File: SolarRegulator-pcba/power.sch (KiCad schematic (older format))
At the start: 59 parts

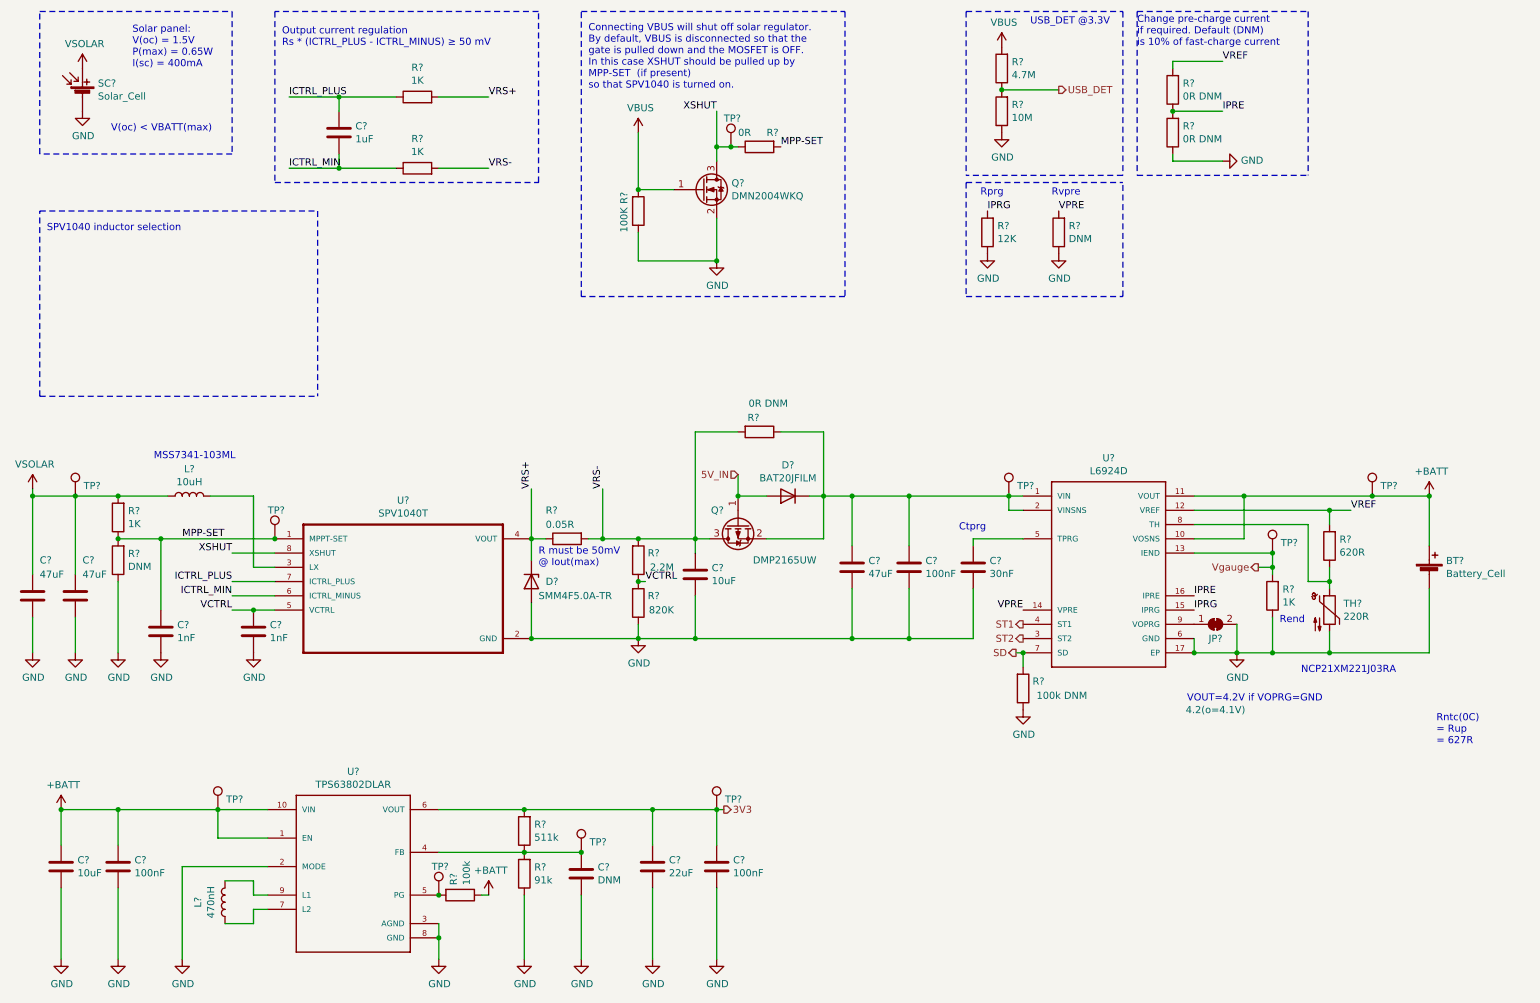
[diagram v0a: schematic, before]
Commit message: Add terminal blocks
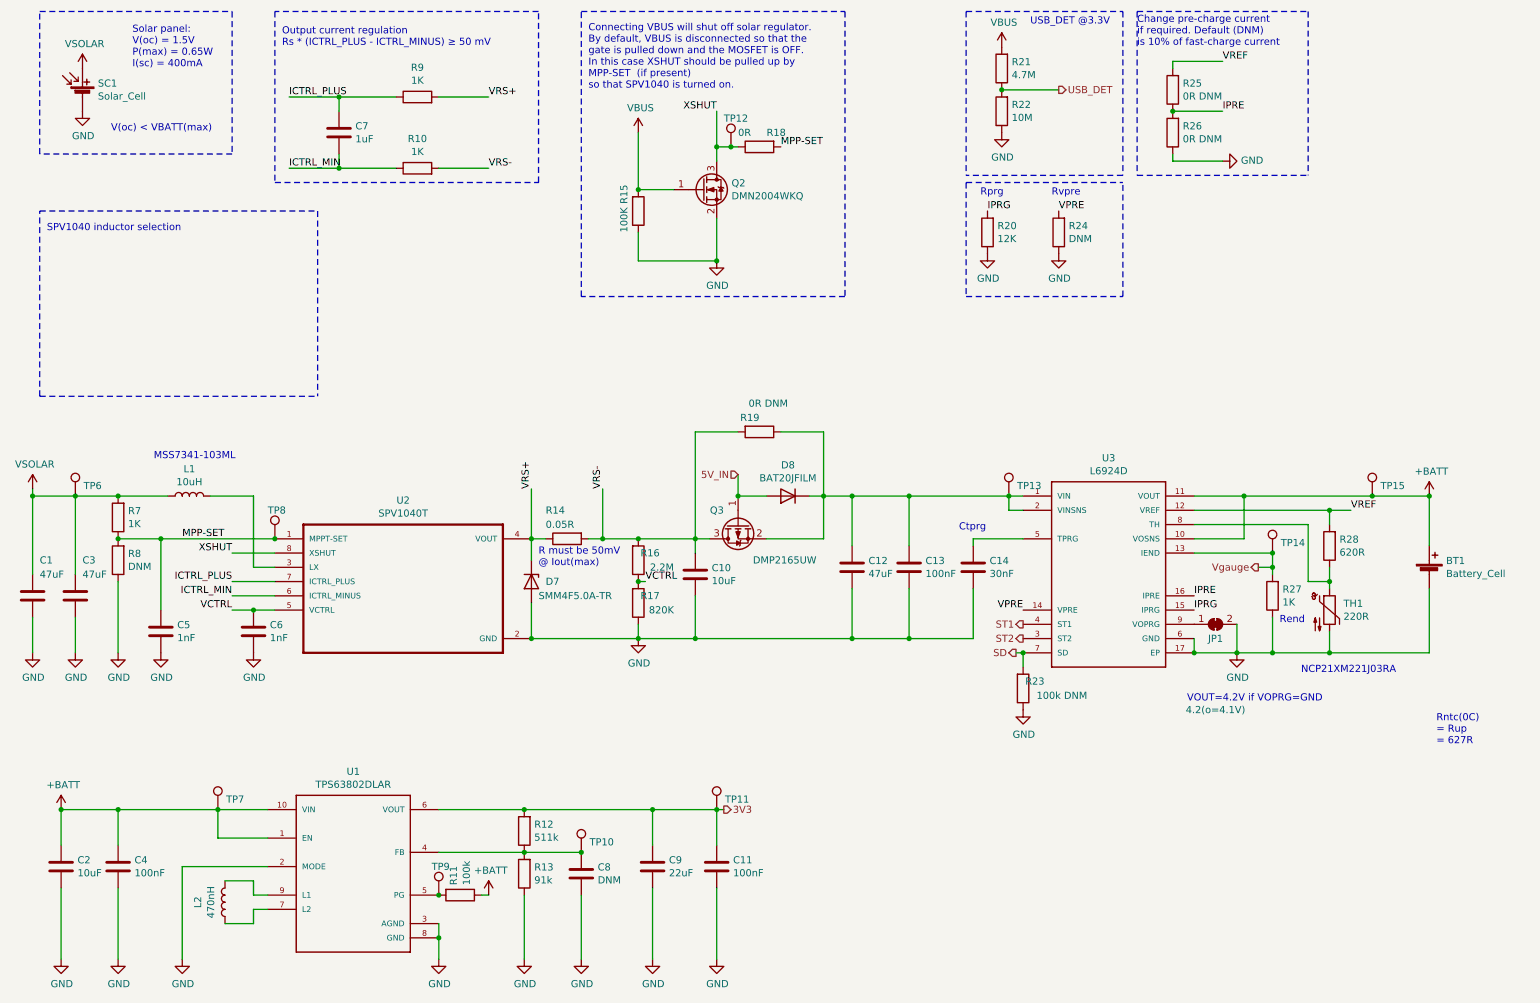
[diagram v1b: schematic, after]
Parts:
- BT1: renamed from BT?; footprint Connector_JST:JST_PH_S2B-PH-SM4-TB_1x02-1MP_P2.00mm_Horizontal -> TerminalBlock_Phoenix:TerminalBlock_Phoenix_MKDS-1,5-2_1x02_P5.00mm_Horizontal
- SC1: renamed from SC?; footprint Connector_JST:JST_PH_S2B-PH-SM4-TB_1x02-1MP_P2.00mm_Horizontal -> TerminalBlock_Phoenix:TerminalBlock_Phoenix_MKDS-1,5-2_1x02_P5.00mm_Horizontal
- gave numbers to parts that had none: 57
